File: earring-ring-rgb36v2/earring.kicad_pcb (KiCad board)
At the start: 2 copper layers, 75 x 92.5 mm, 60 parts, among them J1 Conn_01x05, Q1 AO3401A, SW1 SW_Push, U2 STM32L031G6Ux

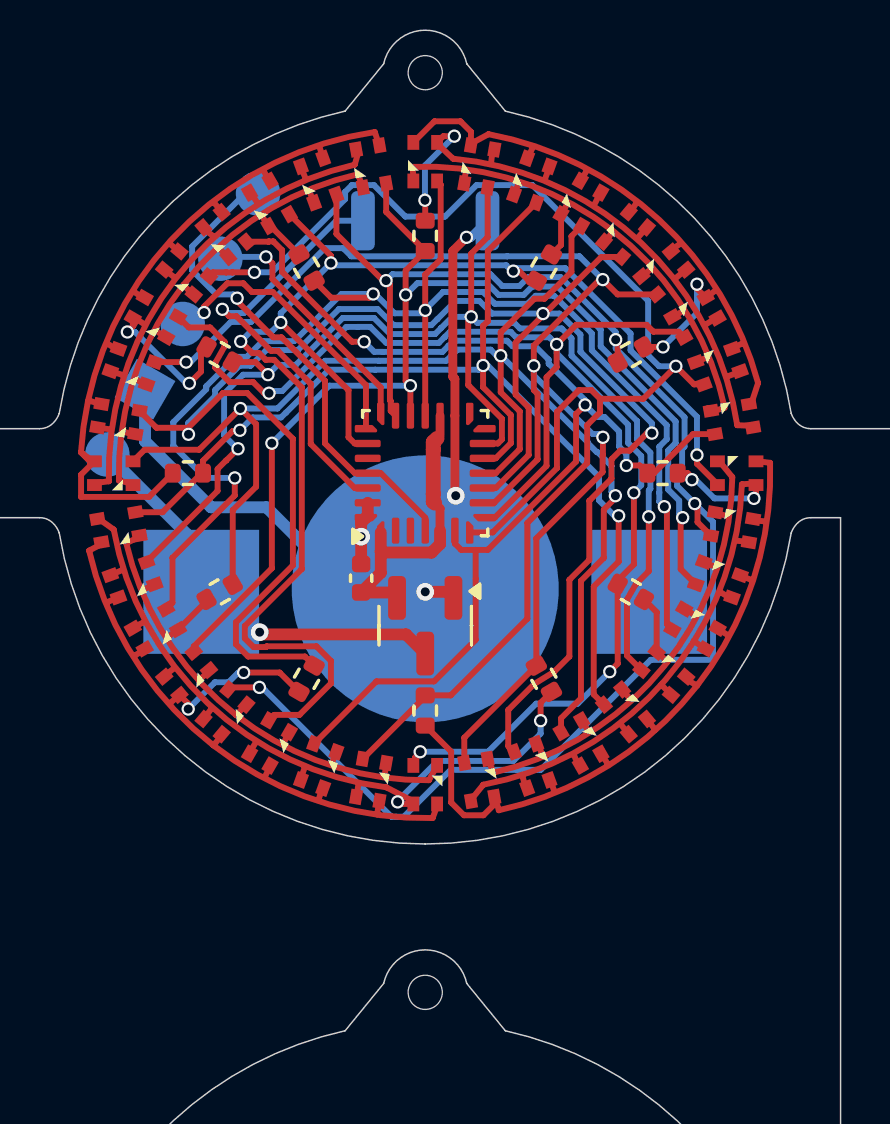
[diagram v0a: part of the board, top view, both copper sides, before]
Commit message: earring-ring-rgb36v2: add phototransistor for light sensing
Can also be used for sending new programs, perhaps?
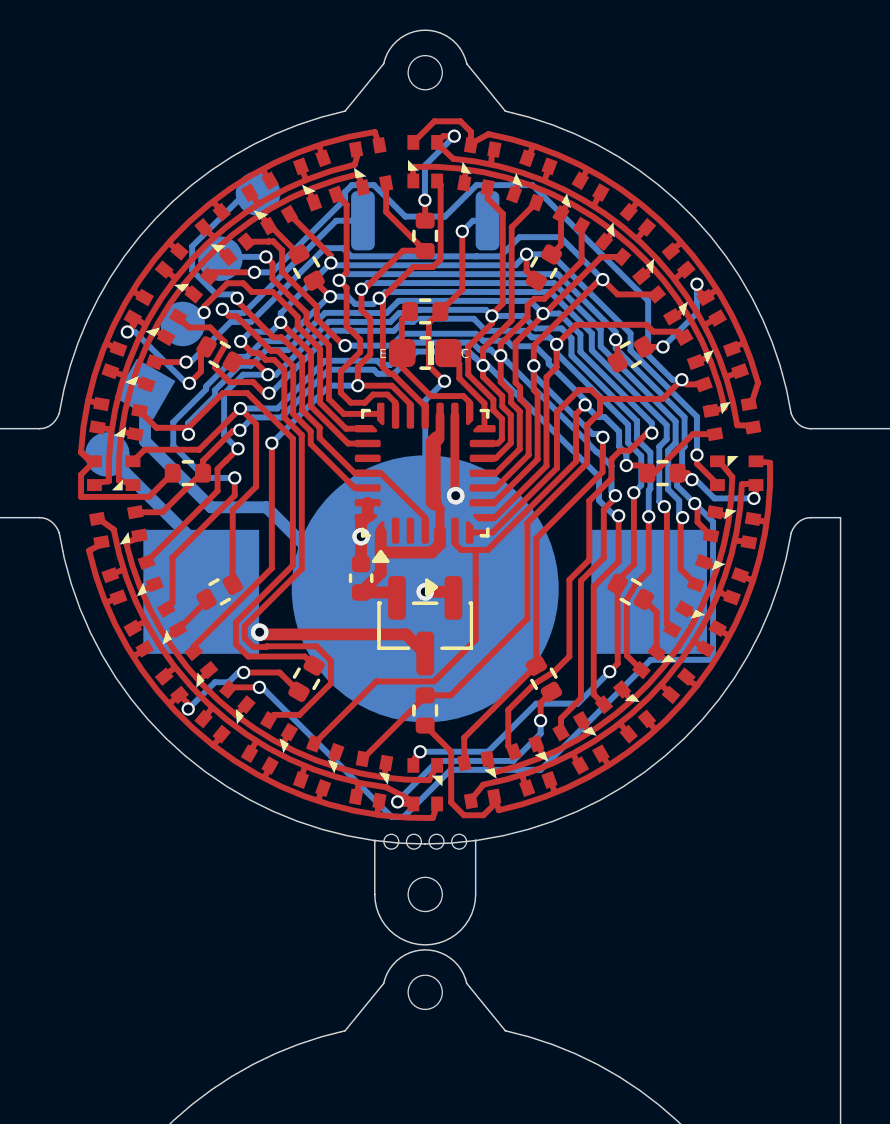
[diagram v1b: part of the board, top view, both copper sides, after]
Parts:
- added Q2: Q_Photo_NPN_EC, Custom:Phototransistor_0603, F.Cu at (0.00, -4.05)
- added R13: 1k, Resistor_SMD:R_0402_1005Metric, F.Cu at (0.00, -5.45)
- added REF**: ToolingHoleWithMouseBytes, Custom:ToolingHoleWithMouseBytes, F.Cu at (0.00, 14.2)
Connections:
- U2 pad 14: unconnected-(U2-PB0-Pad14) -> PHOTO_VCC
- U2 pad 15: unconnected-(U2-PB1-Pad15) -> PHOTO_SENSE
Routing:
- net GND: track 28.9 -> 35.8 mm, vias 4 -> 5
- net PHOTO_SENSE: track 0.00 -> 5.16 mm
- net A2: track 52.3 -> 55.4 mm
- net PHOTO_VCC: track 0.00 -> 3.05 mm
- net A3: track 40.1 -> 42.3 mm
- net SWDIO: track 8.46 -> 9.18 mm
- net A9: track 45.2 -> 45.7 mm
- net A6: track 38.4 -> 38.9 mm
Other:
- board text added: "v1.1"
- board text removed: "v1.0"

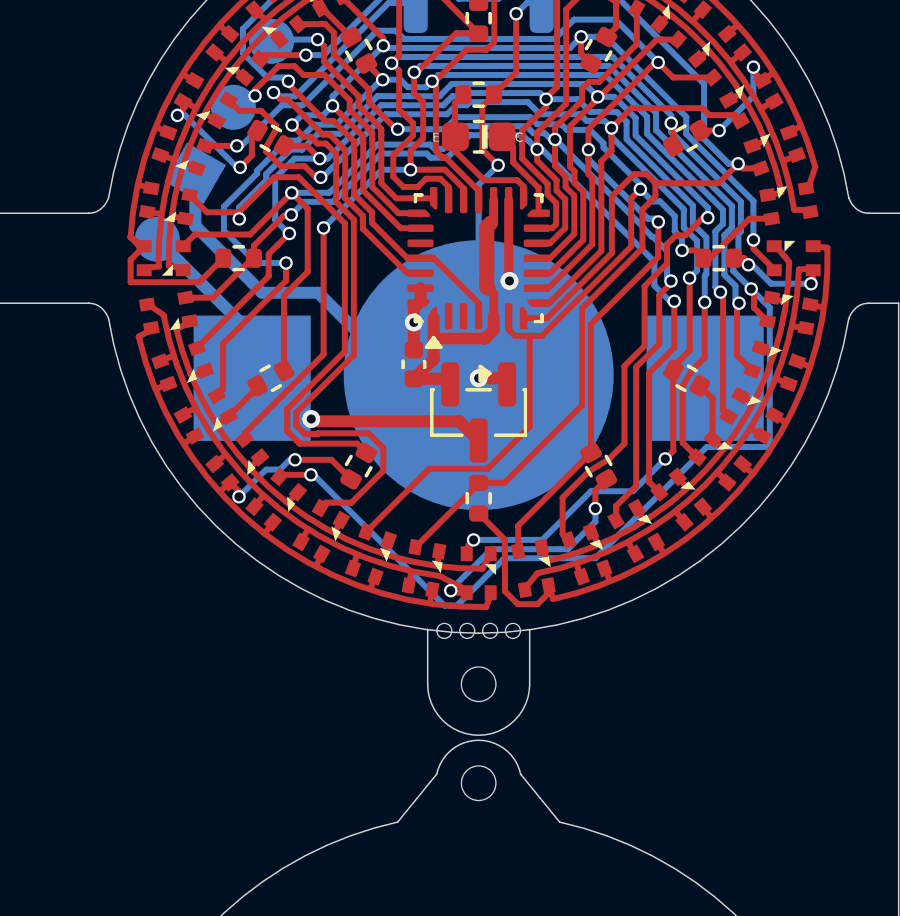
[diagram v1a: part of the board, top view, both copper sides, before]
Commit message: earring-ring-rgb36v2: add 32768Hz crystal oscillator
No idea whether this is correct, might need some additional checking.
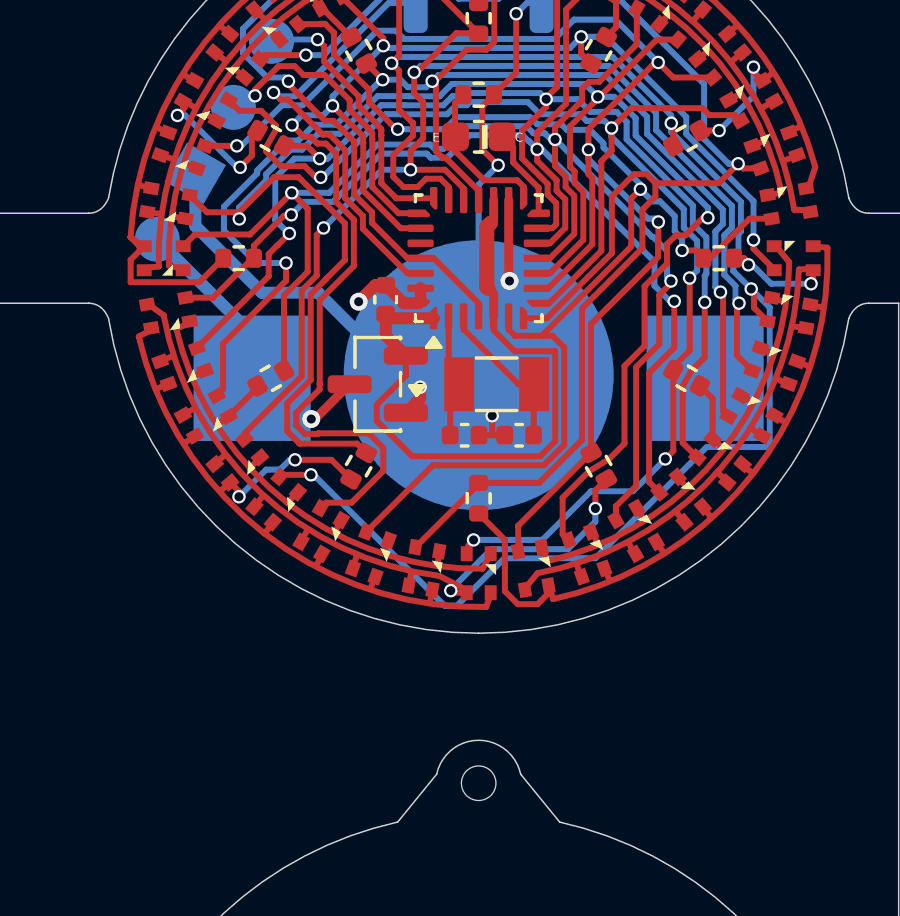
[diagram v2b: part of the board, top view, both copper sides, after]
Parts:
- removed REF**: ToolingHoleWithMouseBytes, Custom:ToolingHoleWithMouseBytes
- added C2: 22pF, Capacitor_SMD:C_0402_1005Metric, F.Cu at (-0.47, 5.90)
- added C3: 22pF, Capacitor_SMD:C_0402_1005Metric, F.Cu at (1.35, 5.90)
- added Y1: Crystal, Crystal:Crystal_SMD_3215-2Pin_3.2x1.5mm, F.Cu at (0.60, 4.20)
- moved Q1 3.49 mm to (-3.36, 4.20), turned to 180 degrees
- moved C1 2.36 mm to (-3.10, 1.38)
- renumbered C2 to C1
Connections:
- U2 pad 2: unconnected-(U2-PC14-Pad2) -> Net-(U2-PC14)
- U2 pad 3: unconnected-(U2-PC15-Pad3) -> Net-(U2-PC15)
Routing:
- net VCC: track 10.2 -> 22.4 mm
- net GND: track 35.8 -> 43.2 mm, vias 5 -> 6
- net Net-(U2-PC15): track 0.00 -> 5.25 mm
- net Net-(U2-PC14): track 0.00 -> 4.23 mm
- net VBAT: track 14.1 -> 9.99 mm
- net A12: track 39.1 -> 41.1 mm
- net A11: track 49.4 -> 50.1 mm
